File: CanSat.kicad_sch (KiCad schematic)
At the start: 40 parts, among them IC1 W25Q128JVPIQ, J1 USB_C_Receptacle, M1 SG-90, SW1 SW_MEC_5E, SW2 SW_MEC_5E, U1 MPU-6050, U6 LM1085-5.0, U7 LM1085-3.3, U8 BMP280, U9 APS6404L-3SQR-ZR

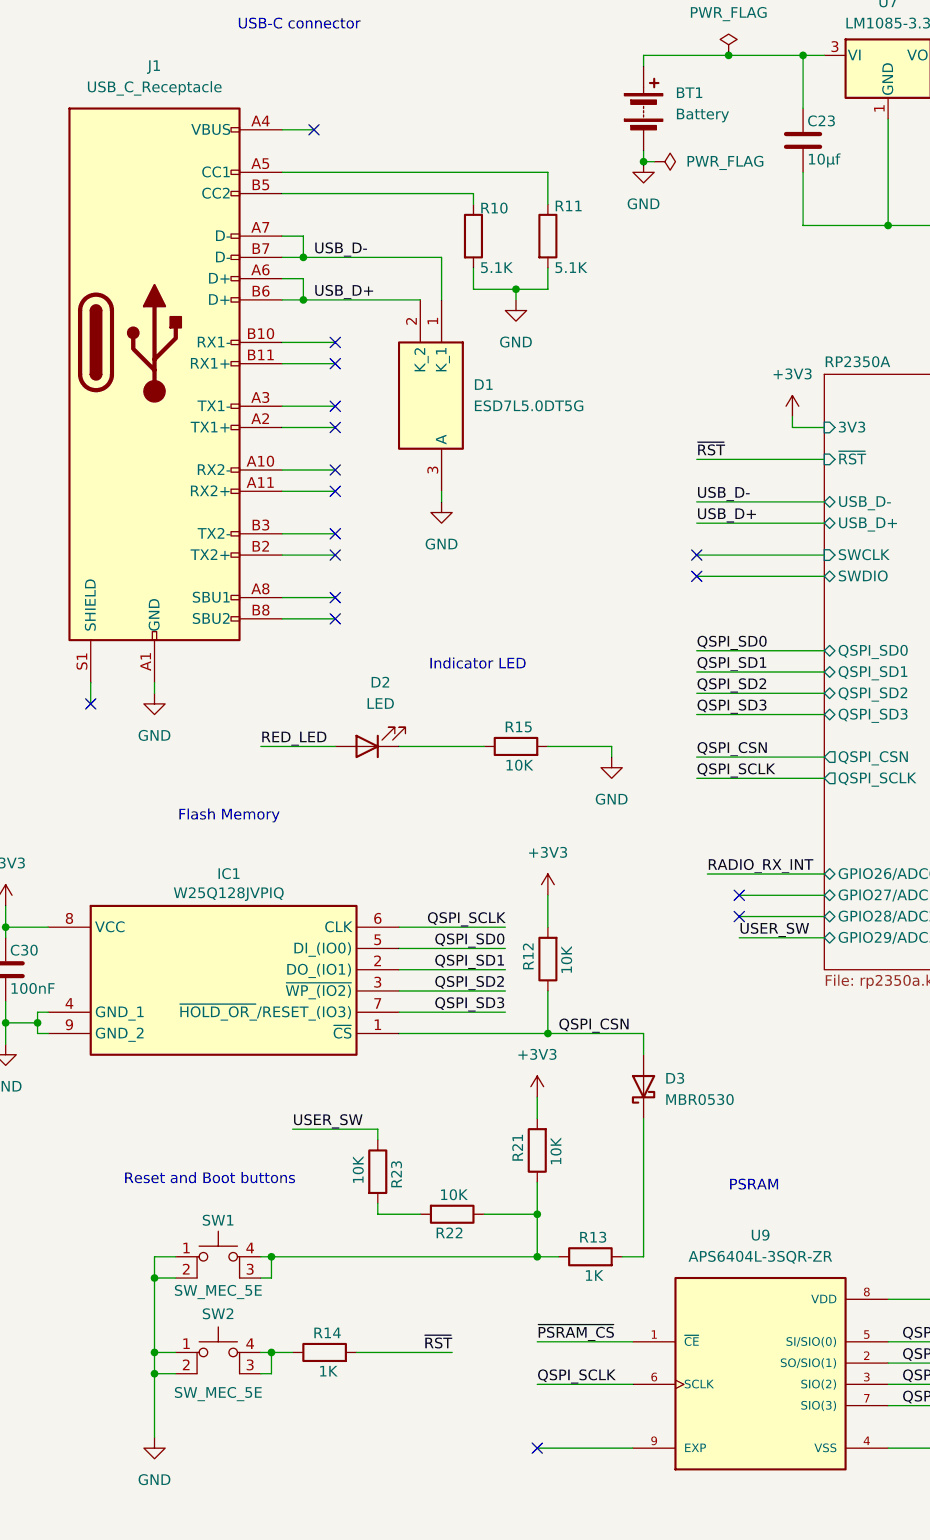
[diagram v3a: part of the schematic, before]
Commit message: Add components to pcb
Added:
3V3 power source
USB-C connector
Flash memory and PSRAM
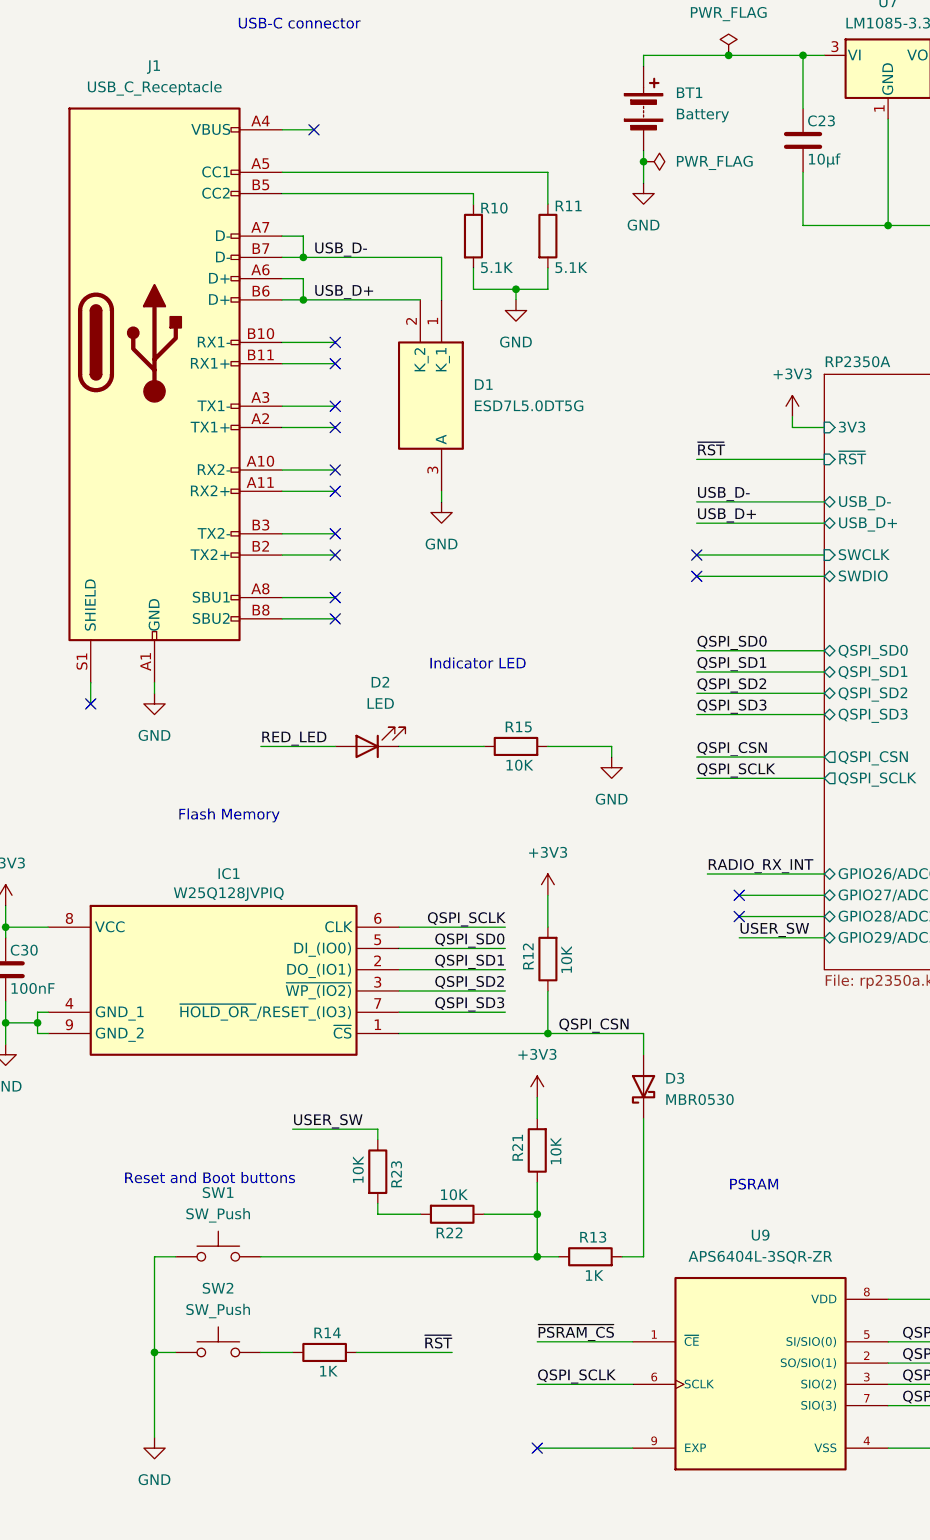
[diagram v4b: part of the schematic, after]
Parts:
- removed SW1, SW2: SW_MEC_5E, Button_Switch_SMD:Panasonic_EVQPUL_EVQPUC, symbol Switch:SW_MEC_5E
- added SW1, SW2: SW_Push, Button_Switch_SMD:SW_Push_1P1T_NO_Vertical_Wuerth_434133025816, symbol Switch:SW_Push
- BZ1: footprint Buzzer_Beeper:PUIAudio_SMT_0825_S_4_R -> Buzzer_Beeper:MagneticBuzzer_Kingstate_KCG0601
- J1: footprint Connector_USB:USB_C_Receptacle_Amphenol_124019772112A -> Connector_USB:USB_C_Receptacle_Amphenol_12401610E4-2A
- M1: footprint (none) -> Connector_PinHeader_1.00mm:PinHeader_1x03_P1.00mm_Vertical
- U3: footprint (none) -> Connector_PinHeader_1.00mm:PinHeader_1x05_P1.00mm_Vertical
- U6: footprint (none) -> LM1085IT-5.0:TO254P1054X470X1955-3
- U7: footprint (none) -> LM1085IT-3.3:TO254P1054X470X1955-3
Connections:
- net GND: now also SW1.1, SW2.1
- net at R13.1, R21.1, R22.1: now also SW1.2
- net at R14.1: now also SW2.2

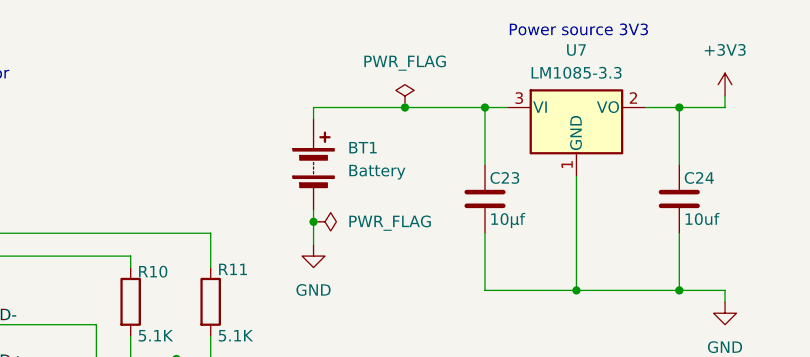
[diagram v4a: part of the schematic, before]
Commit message: Connected LoRa
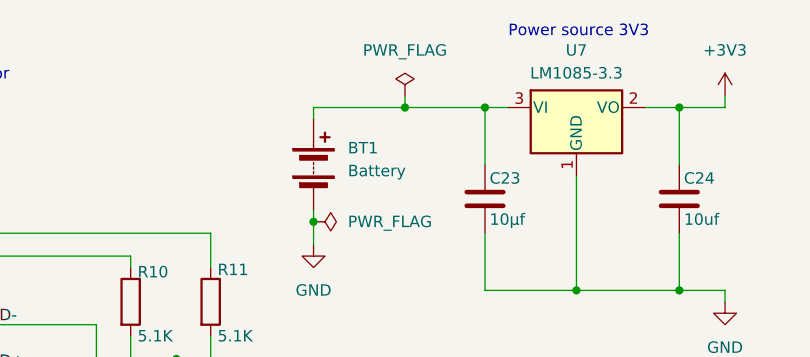
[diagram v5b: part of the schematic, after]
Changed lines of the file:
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@@
 	(wire
 		(pts
+			(xy 105.41 22.86) (xy 105.41 24.13)
+		)
+		(stroke
+			(width 0)
+			(type default)
+		)
+	)
+	(wire
+		(pts
 			(xy 165.1 99.06) (xy 186.69 99.06)
 		)
@@
 	(symbol
 		(lib_id "power:PWR_FLAG")
-		(at 105.41 24.13 0)
+		(at 105.41 22.86 0)
 		(unit 1)
 		(exclude_from_sim no)
@@
 		(fields_autoplaced yes)
 		(property "Reference" "#FLG04"
-			(at 105.41 22.225 0)
+			(at 105.41 20.955 0)
 			(effects
 				(font
@@
 		)
 		(property "Value" "PWR_FLAG"
-			(at 105.41 19.05 0)
+			(at 105.41 17.78 0)
 			(effects
 				(font
@@
 		)
 		(property "Footprint" ""
-			(at 105.41 24.13 0)
+			(at 105.41 22.86 0)
 			(effects
 				(font
@@
 		)
 		(property "Datasheet" "~"
-			(at 105.41 24.13 0)
+			(at 105.41 22.86 0)
 			(effects
 				(font
@@
 		)
 		(property "Description" "Special symbol for telling ERC where power comes from"
-			(at 105.41 24.13 0)
+			(at 105.41 22.86 0)
 			(effects
 				(font

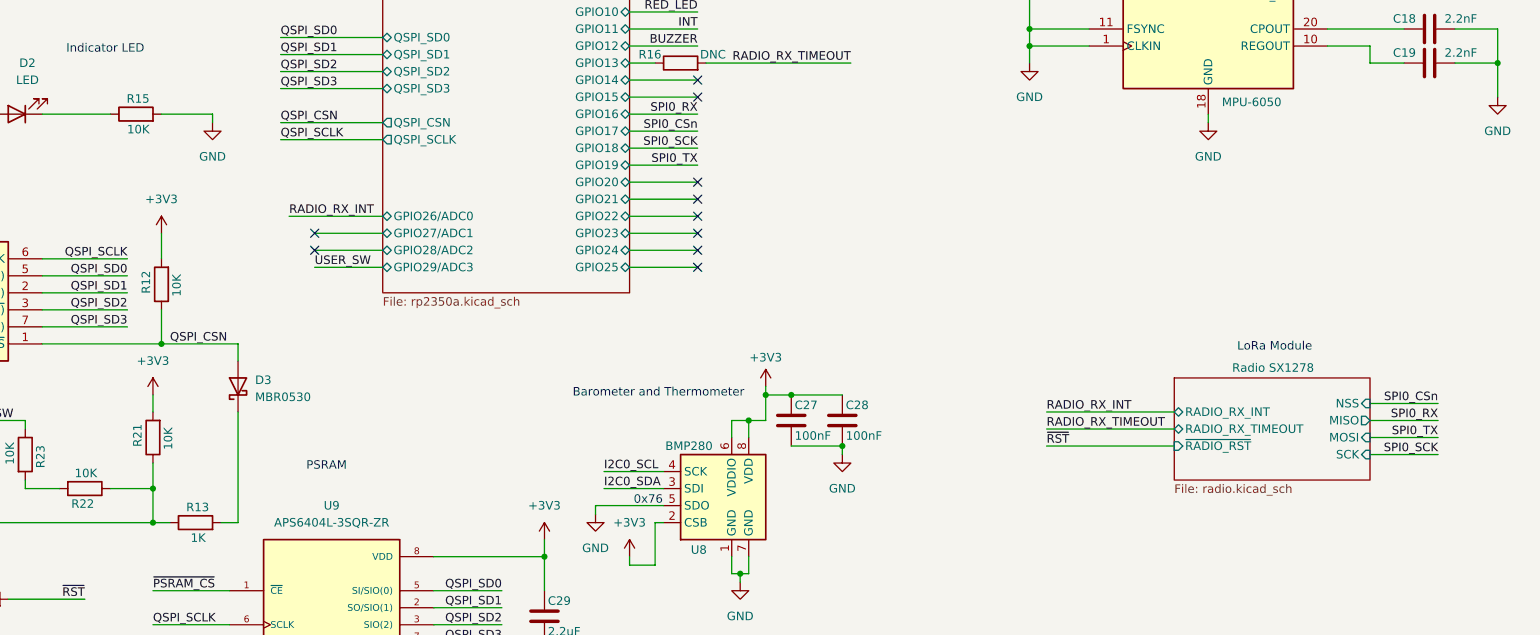
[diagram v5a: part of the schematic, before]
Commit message: Changed LoRa module to RFM98W 433MHz
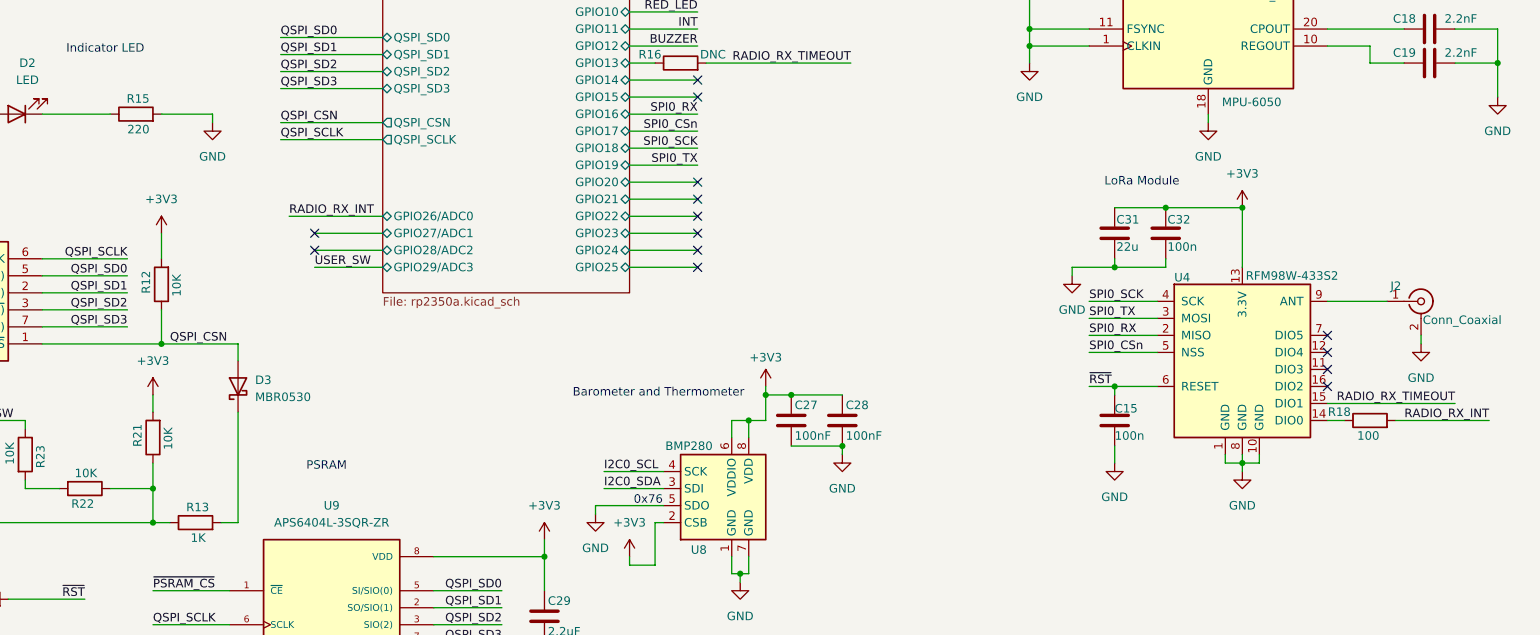
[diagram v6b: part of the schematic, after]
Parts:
- added C15, C32: 100n, Capacitor_Tantalum_SMD:CP_EIA-2012-15_AVX-P, symbol Device:C
- added C31: 22u, Capacitor_Tantalum_SMD:CP_EIA-2012-15_AVX-P, symbol Device:C
- added J2: Conn_Coaxial, Connector_Coaxial:SMA_Amphenol_901-144_Vertical, symbol Connector:Conn_Coaxial
- added R18: 100, Resistor_SMD:R_0805_2012Metric, symbol Device:R
- added U4: RFM98W-433S2, RF_Module:HOPERF_RFM9XW_THT, symbol RF_Module:RFM98W-433S2
- R15: value 10K -> 220
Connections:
- net +3V3: now also C31.1, C32.1, U4.13 (3.3V)
- net GND: now also C15.2, C31.2, C32.2, J2.2 (Ext), U4.1 (GND), U4.10 (GND), U4.8 (GND)
- net RADIO_RX_INT: now also R18.2
- net RADIO_RX_TIMEOUT: now also U4.15 (DIO1)
- net SPI0_CSn: now also U4.5 (NSS)
- net SPI0_RX: now also U4.2 (MISO)
- net SPI0_SCK: now also U4.4 (SCK)
- net SPI0_TX: now also U4.3 (MOSI)
- net ~{RST}: now also C15.1, U4.6 (RESET)
- new net: J2.1 (In), U4.9 (ANT)
- new net: R18.1, U4.14 (DIO0)
- no-connect marks 32 -> 36
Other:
- removed sheet Radio SX1278
